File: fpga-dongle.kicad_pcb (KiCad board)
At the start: 2 copper layers, 85.8 x 137 mm, 66 parts, among them P1 USB_PWR, P2 PGM, P3 right, P4 left, P5 CONN_01X40, P6 CONN_01X40, SW1 T1107A(6x3,8x2,5MM), U1 W25Q16BVSSIG(SOIC-8_208mil), U2 sc189(Z) 3.3v, U3 sc189(C) 1.2v, U4 iCE40-HX4K-TQ144, U5 AS4C16M16S

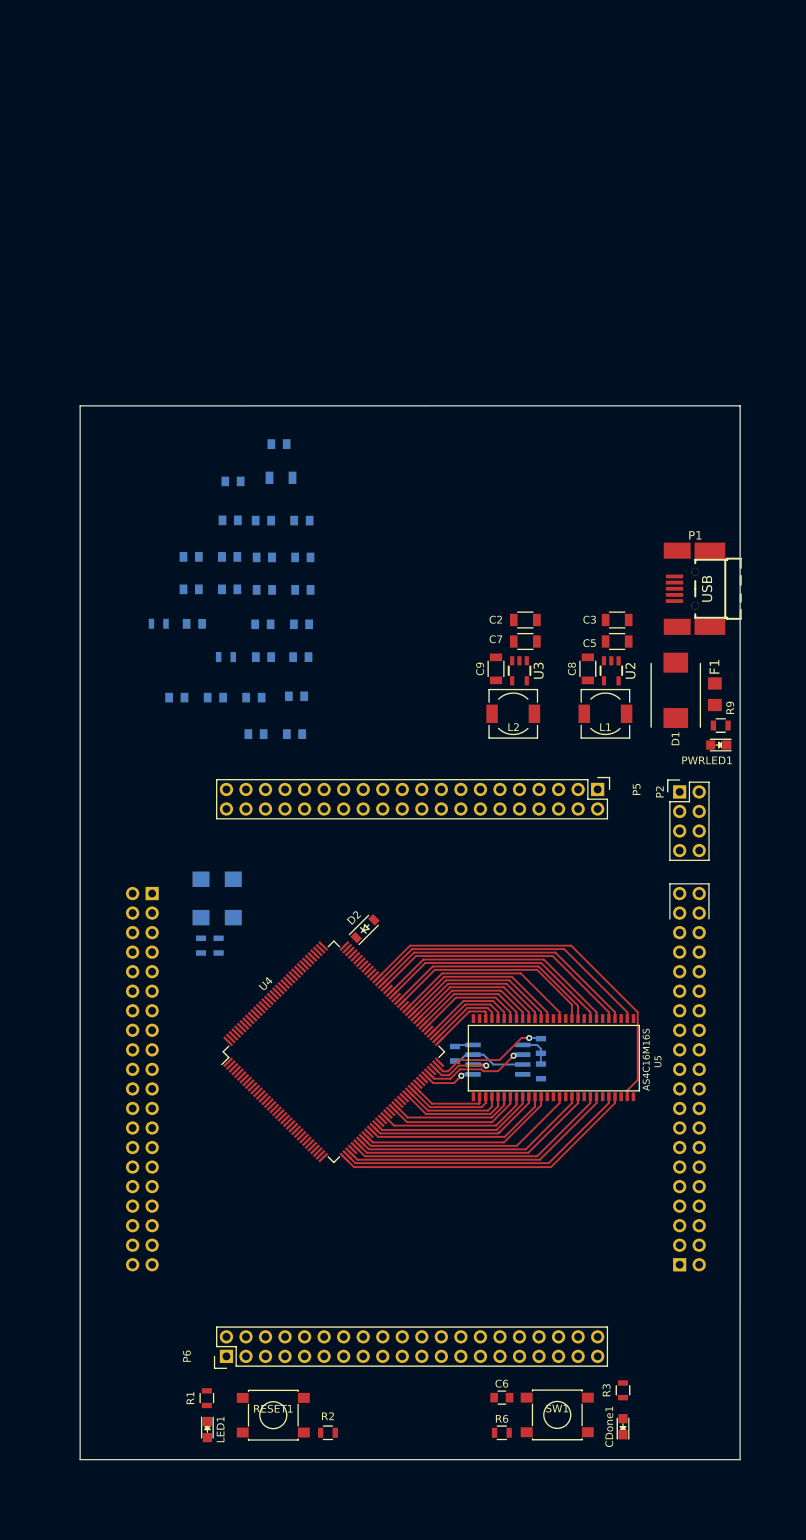
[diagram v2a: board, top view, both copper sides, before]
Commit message: Added SPI programmer with LPC11U35 as MSC
Signed-off-by: Martin Ribelotta <martinribelotta@gmail.com>
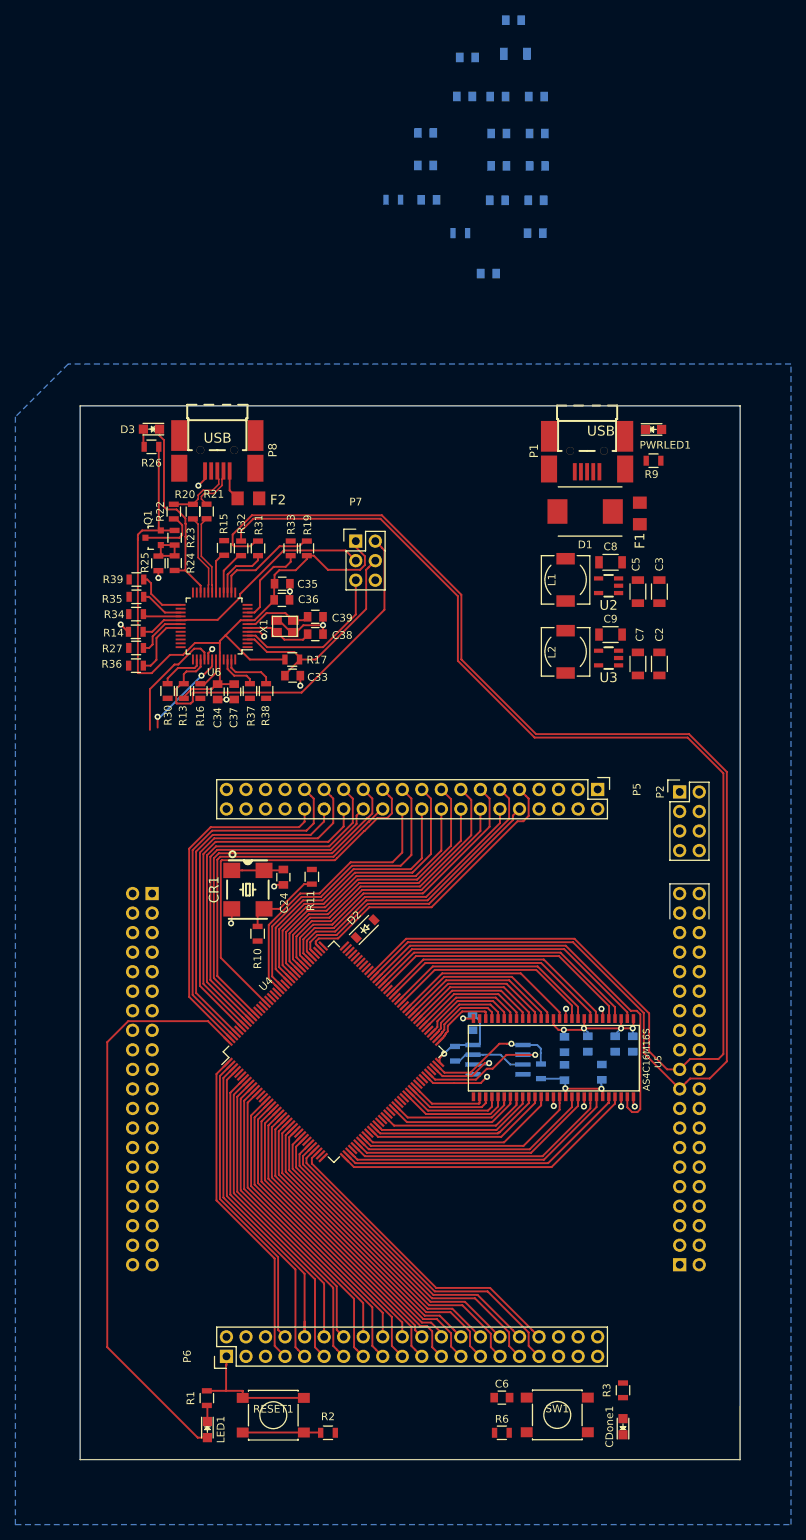
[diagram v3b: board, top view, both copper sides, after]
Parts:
- removed R7: 22R, Resistors_SMD:R_0805
- added C33: 100nF, Capacitors_SMD:C_0805, F.Cu at (42.9, 52.7)
- added C34: 100nF, Capacitors_SMD:C_0805, F.Cu at (33.1, 54.8)
- added C35: 10nF, Capacitors_SMD:C_0805, F.Cu at (41.5, 40.8)
- added C36: 100nF, Capacitors_SMD:C_0805, F.Cu at (41.5, 42.9)
- added C37: 10nF, Capacitors_SMD:C_0805, F.Cu at (35.3, 54.8)
- added C38: 18pF, Capacitors_SMD:C_0805, F.Cu at (45.9, 47.3)
- added C39: 18pF, Capacitors_SMD:C_0805, F.Cu at (45.9, 45.0)
- added D3: LED, LEDs:LED-0805, F.Cu at (24.6, 20.6)
- added F2: 1A, OLIMEX_Devices-FP:FUSE-1206, F.Cu at (37.1, 29.6)
- added P7: DBG_SWD, Pin_Headers:Pin_Header_Straight_2x03, F.Cu at (51.1, 35.2)
- added P8: USB_PWR, OLIMEX_Connectors-FP:USB_Mini-B-NOSILK, F.Cu at (33.1, 23.4)
- added Q1: BC857, TO_SOT_Packages_SMD:SOT-23, F.Cu at (24.8, 34.8)
- added R13: 24k, Resistors_SMD:R_0805, F.Cu at (28.8, 54.7)
- added R14: 24k, Resistors_SMD:R_0805, F.Cu at (22.5, 47.0)
- added R15: 22R, Resistors_SMD:R_0805, F.Cu at (34.0, 36.1)
- added R16: 22R, Resistors_SMD:R_0805, F.Cu at (30.9, 54.7)
- added R17: 10k, Resistors_SMD:R_0805, F.Cu at (42.9, 50.6)
- added R19: 2k, Resistors_SMD:R_0805, F.Cu at (44.8, 36.1)
- added R20: 33, Resistors_SMD:R_0805, F.Cu at (29.9, 31.4)
- added R21: 33, Resistors_SMD:R_0805, F.Cu at (31.7, 31.4)
- added R22: 1.5k, Resistors_SMD:R_0805, F.Cu at (27.4, 31.4)
- added R23: 24k, Resistors_SMD:R_0805, F.Cu at (27.6, 34.8)
- added R24: 2k, Resistors_SMD:R_0805, F.Cu at (27.6, 38.1)
- added R25: UL, Resistors_SMD:R_0805, F.Cu at (25.4, 38.1)
- added R26: 2k, Resistors_SMD:R_0805, F.Cu at (24.6, 22.9)
- added R27: 22R, Resistors_SMD:R_0805, F.Cu at (22.6, 49.1)
- added R30: 22R, Resistors_SMD:R_0805, F.Cu at (26.6, 54.7)
- added R31: 100R, Resistors_SMD:R_0805, F.Cu at (38.4, 36.1)
- added R32: 100R, Resistors_SMD:R_0805, F.Cu at (36.2, 36.1)
- added R33: 100R, Resistors_SMD:R_0805, F.Cu at (42.6, 36.1)
- added R34: 100R, Resistors_SMD:R_0805, F.Cu at (22.5, 44.7)
- added R35: 100R, Resistors_SMD:R_0805, F.Cu at (22.6, 42.5)
- added R36: 100R, Resistors_SMD:R_0805, F.Cu at (22.5, 51.4)
- added R37: 100R, Resistors_SMD:R_0805, F.Cu at (37.4, 54.7)
- added R38: 100R, Resistors_SMD:R_0805, F.Cu at (39.5, 54.7)
- added R39: 100R, Resistors_SMD:R_0805, F.Cu at (22.6, 40.2)
- added U6: LPC11U35FBD48, Housings_QFP:LQFP-48_7x7mm_Pitch0.5mm, F.Cu at (32.7, 46.2)
- added X1: 12MHz, Crystals_Oscillators_SMD:crystal_FA238-TSX3225, F.Cu at (41.9, 46.3)
- C24, CR1, R10, R11: moved to F.Cu
- moved C29 79.2 mm to (83.1, 104.2), turned to 90 degrees
- moved C23 74.4 mm to (87.1, 100.6), turned to 270 degrees
- moved C17 68.8 mm to (84.8, 100.6), turned to 270 degrees
- moved C1 63.0 mm to (74.6, -22.6)
- moved C10 63.0 mm to (71.6, -32.5)
- moved C13 63.0 mm to (65.6, -27.7)
- moved C14 63.0 mm to (74.4, -4.83)
- moved C15 63.0 mm to (68.3, 0.43)
- moved C16 63.0 mm to (69.6, -22.6)
- moved C18 63.0 mm to (74.7, -13.6)
- moved C25 63.0 mm to (69.7, -13.6)
- moved C26 63.0 mm to (65.3, -22.6)
- moved C28 63.0 mm to (60.2, -17.9)
- moved C31 63.0 mm to (74.5, -9.10)
- moved C32 63.0 mm to (69.5, -9.10)
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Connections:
- R5 pad 1: Net-(R5-Pad1) -> /iCE40-SS_B
- U1 pad 1: Net-(R5-Pad1) -> /iCE40-SS_B
- U4 pad 104: (no net) -> /SPI_CLK
- U4 pad 105: (no net) -> /RxD
- U4 pad 106: (no net) -> /TxD
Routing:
- net /I2C_SDA: track 0.00 -> 186.7 mm
- net /I2C_SCL: track 0.00 -> 178.1 mm
- net +3V3: track 2.43 -> 151.6 mm, vias 0 -> 8
- net /LED1: track 0.00 -> 75.5 mm
- net GND: track 0.00 -> 53.8 mm, vias 0 -> 17
- net /DBG_SWDIO: track 0.00 -> 50.1 mm
- net /FPGA_IO_BANK1_18: track 0.00 -> 49.4 mm
- net /FPGA_IO_BANK1_14: track 0.00 -> 49.3 mm
- net /FPGA_IO_BANK1_16: track 0.00 -> 49.3 mm
- net /FPGA_IO_BANK1_20: track 0.00 -> 48.8 mm
- net /FPGA_IO_BANK1_22: track 0.00 -> 48.4 mm
- net /FPGA_IO_BANK1_19: track 0.00 -> 46.4 mm
- net /FPGA_IO_BANK1_15: track 0.00 -> 46.3 mm
- net /FPGA_IO_BANK1_17: track 0.00 -> 46.3 mm
- net /FPGA_IO_BANK1_21: track 0.00 -> 45.6 mm
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- added copper zone on B.Cu, net GND

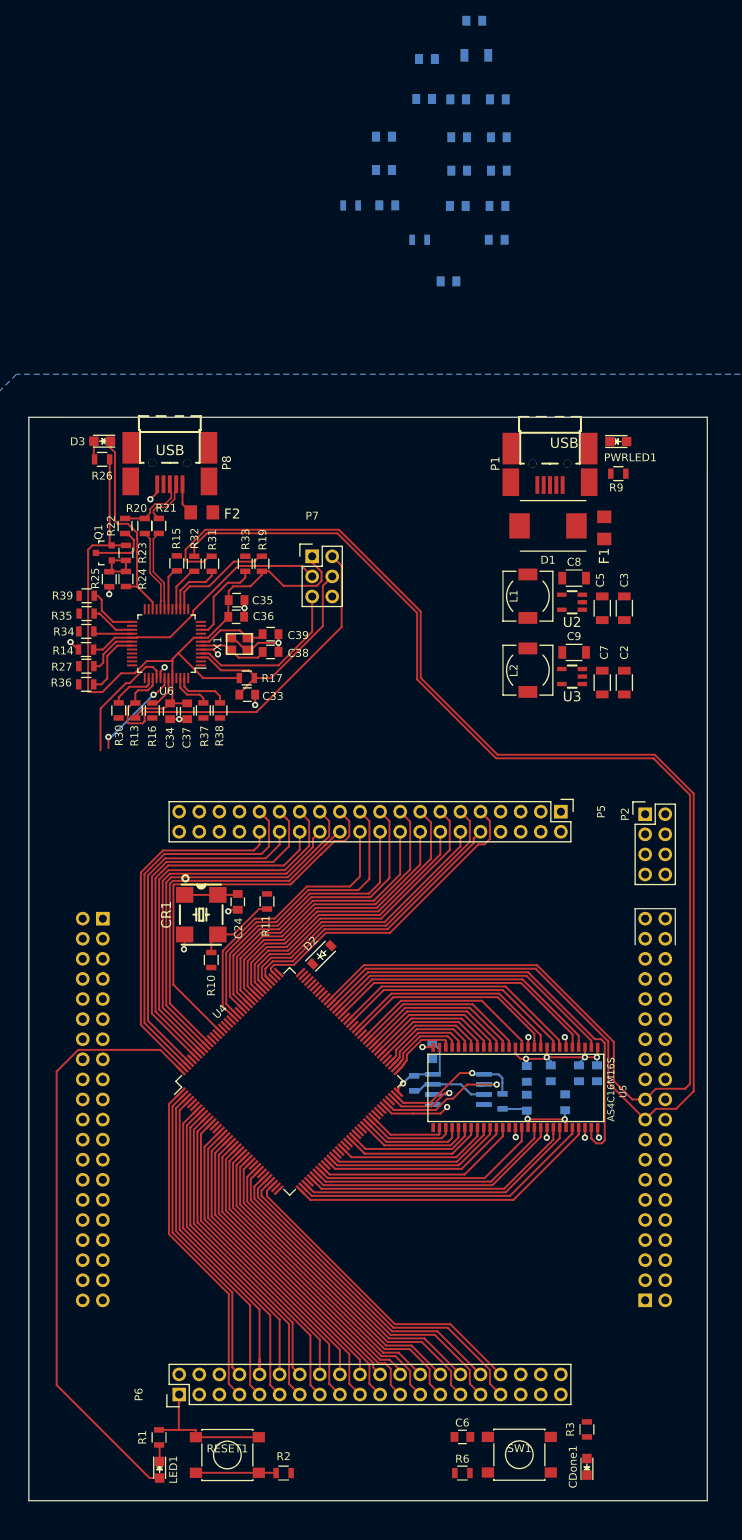
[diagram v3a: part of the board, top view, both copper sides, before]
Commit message: Reroute SDRAM, connect to EDU-CIAA conenctor, fix schematic net tames
Signed-off-by: Martin Ribelotta <martinribelotta@gmail.com>
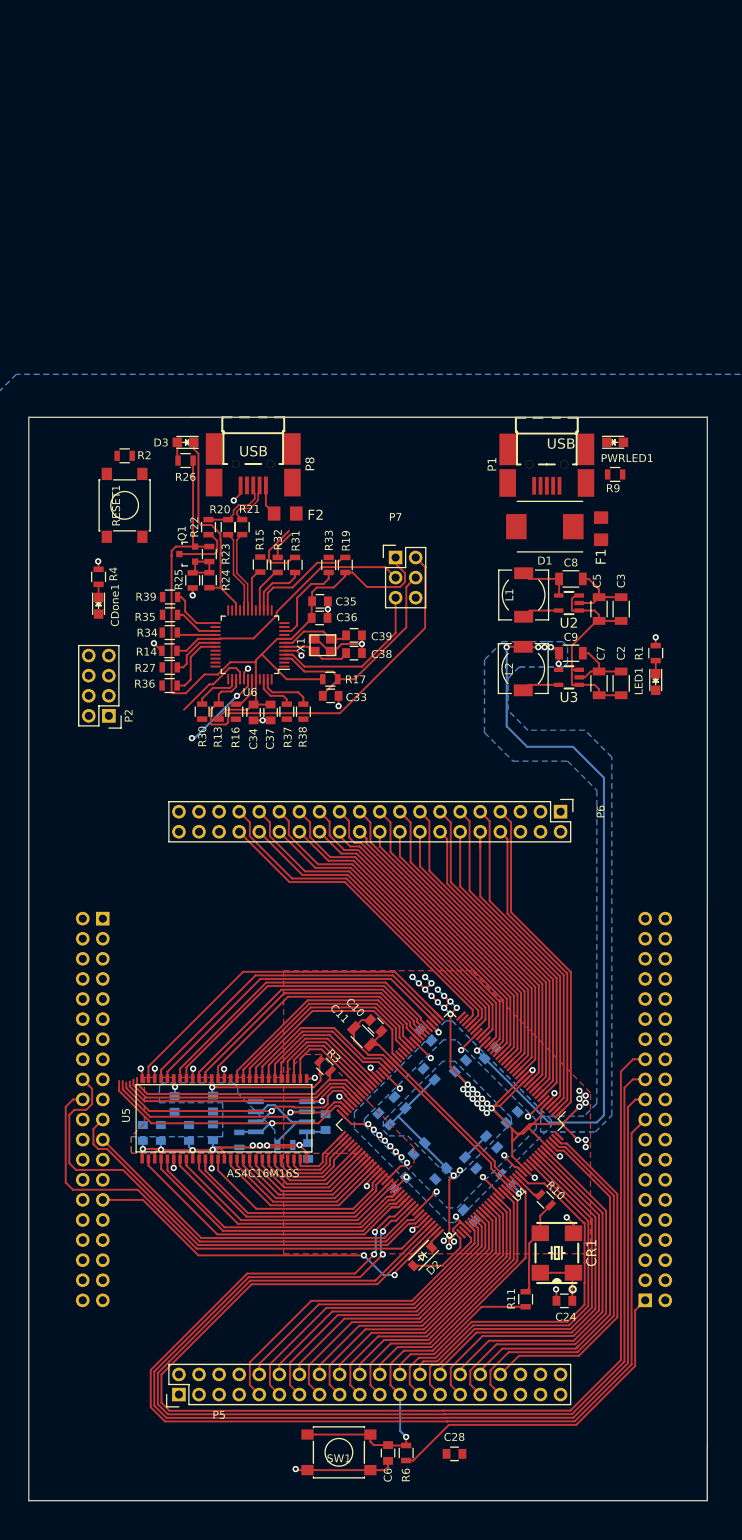
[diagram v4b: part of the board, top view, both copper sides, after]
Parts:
- C10, C11, C28, R4: moved to F.Cu
- moved C28 166.8 mm to (69.1, 148.7), turned to 0 degrees
- moved C13 146.3 mm to (71.0, 118.5), turned to 315 degrees
- moved R2 130.2 mm to (27.4, 22.5)
- moved C26 129.1 mm to (60.2, 106.3), turned to 315 degrees
- moved C10 127.7 mm to (59.1, 94.5), turned to 135 degrees
- moved C16 127.1 mm to (62.2, 104.3), turned to 315 degrees
- moved CDone1 125.2 mm to (24.1, 41.5), turned to 270 degrees
- moved C11 124.9 mm to (57.5, 95.9), turned to 135 degrees
- moved R12 124.7 mm to (75.7, 114.0), turned to 315 degrees
- moved C18 124.1 mm to (64.7, 110.1), turned to 45 degrees
- moved C19 123.9 mm to (76.4, 106.2), turned to 225 degrees
- moved C1 123.6 mm to (65.9, 100.7), turned to 135 degrees
- moved C25 122.9 mm to (73.8, 109.3), turned to 135 degrees
- moved C31 122.6 mm to (67.4, 113.3), turned to 45 degrees
- moved C32 121.0 mm to (71.2, 111.9), turned to 135 degrees
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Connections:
- P3 pad 20: (no net) -> /SPI_CLK
- P4 pad 23: (no net) -> /RxD
- P4 pad 25: (no net) -> /TxD
- P5 pad 23: /FPGA_IO_BANK1_14 -> /BUT1
- P5 pad 24: /FPGA_IO_BANK1_15 -> /EXTCLK
- P5 pad 25: /FPGA_IO_BANK1_16 -> /FPGA_IO_BANK1_14
- P5 pad 26: /FPGA_IO_BANK1_17 -> /FPGA_IO_BANK1_15
- P5 pad 27: /FPGA_IO_BANK1_18 -> /FPGA_IO_BANK1_16
- P5 pad 28: /FPGA_IO_BANK1_19 -> /FPGA_IO_BANK1_17
- P5 pad 29: /FPGA_IO_BANK1_20 -> /FPGA_IO_BANK1_18
- P5 pad 30: /FPGA_IO_BANK1_21 -> /FPGA_IO_BANK1_19
- P5 pad 31: /FPGA_IO_BANK1_22 -> /FPGA_IO_BANK1_20
- P5 pad 32: /FPGA_IO_BANK1_23 -> /FPGA_IO_BANK1_21
- P5 pad 33: (no net) -> /FPGA_IO_BANK1_22
- P5 pad 34: (no net) -> /FPGA_IO_BANK1_23
- R11 pad 1: (no net) -> /EXTCLK
- U4 pad 37: /RAM_D14 -> /RAM_D15
- U4 pad 38: /RAM_D13 -> /RAM_D14
- U4 pad 39: /RAM_D12 -> /RAM_D13
- U4 pad 41: /RAM_D11 -> /RAM_D12
- U4 pad 42: /RAM_D10 -> /RAM_D11
- U4 pad 43: /RAM_D9 -> /RAM_D10
- U4 pad 44: /RAM_D8 -> /RAM_D9
- U4 pad 45: /RAM_DQMH -> /RAM_D8
- U4 pad 47: /RAM_CLK -> /RAM_DQMH
- U4 pad 48: /RAM_CKE -> /RAM_CLK
- U4 pad 49: /RAM_A13 -> /RAM_CKE
- U4 pad 52: /RAM_A12 -> /RAM_A13
- U4 pad 55: /RAM_A10 -> /RAM_A12
- U4 pad 56: /RAM_A9 -> /RAM_A10
- U4 pad 60: /RAM_A8 -> /RAM_A9
- U4 pad 61: /RAM_A7 -> /RAM_A8
- U4 pad 62: /RAM_A6 -> /RAM_A7
- U4 pad 63: /RAM_A5 -> /RAM_A6
- U4 pad 64: /RAM_A4 -> /RAM_A5
- U4 pad 73: /RAM_A3 -> /RAM_A4
- U4 pad 74: /RAM_A2 -> /RAM_A3
- U4 pad 75: /RAM_A1 -> /RAM_A2
- U4 pad 76: /RAM_A11 -> /RAM_A1
- U4 pad 78: /RAM_A15 -> /RAM_A11
- U4 pad 79: /RAM_A14 -> /RAM_A15
- U4 pad 80: /RAM_CS -> /RAM_A14
- U4 pad 81: /RAM_RAS -> /RAM_CS
- U4 pad 82: /RAM_CAS -> /RAM_RAS
- U4 pad 83: /RAM_RDnWR -> /RAM_CAS
- U4 pad 84: /RAM_DQML -> /RAM_RDnWR
- U4 pad 85: /RAM_D7 -> /RAM_DQML
- U4 pad 87: /RAM_D6 -> /RAM_D7
- U4 pad 88: /RAM_D5 -> /RAM_D6
- U4 pad 90: /RAM_D4 -> /RAM_D5
- U4 pad 91: /RAM_D3 -> /RAM_D4
- U4 pad 93: /RAM_D2 -> /RAM_D3
- U4 pad 94: /RAM_D1 -> /RAM_D2
- U4 pad 95: /RAM_D0 -> /RAM_D1
- U4 pad 96: /RAM_D15 -> /RAM_D0
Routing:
- net GND: track 53.8 -> 216.1 mm, vias 17 -> 68
- net /TxD: track 0.00 -> 147.0 mm
- net /RxD: track 0.00 -> 146.2 mm
- net +1V2: track 0.00 -> 116.4 mm, vias 0 -> 9
- net +3V3: track 151.6 -> 263.5 mm, vias 8 -> 25
- net /LED1: track 75.5 -> 0.00 mm
- net /SPI_MISO: track 0.00 -> 63.6 mm
- net /SPI_CLK: track 0.00 -> 62.8 mm
- net /BUT1: track 0.00 -> 57.7 mm, vias 0 -> 1
- net /SPI_MOSI: track 0.00 -> 51.4 mm
- net /GPIO0: track 0.00 -> 48.7 mm, vias 0 -> 2
- net /SPI_CS: track 0.00 -> 46.0 mm
- net /VCCPLL: track 0.00 -> 34.9 mm, vias 0 -> 1
- net /I2C_SDA: track 186.7 -> 152.7 mm, vias 0 -> 2
- net /I2C_SCL: track 178.1 -> 149.5 mm, vias 0 -> 2
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- added copper zone on B.Cu, net +1V2
- added copper zone on B.Cu, net +3V3
- added copper zone on F.Cu, net +3V3
- added copper zone on F.Cu, net GND
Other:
- outline, holes or cut-outs redrawn
